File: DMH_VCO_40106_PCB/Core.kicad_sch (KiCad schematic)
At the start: 73 parts, among them Q1 BC558, Q2 BC548, Q7 MMBFJ113, U1 40106, U2 TL074, U3 TL074, U4 TL074

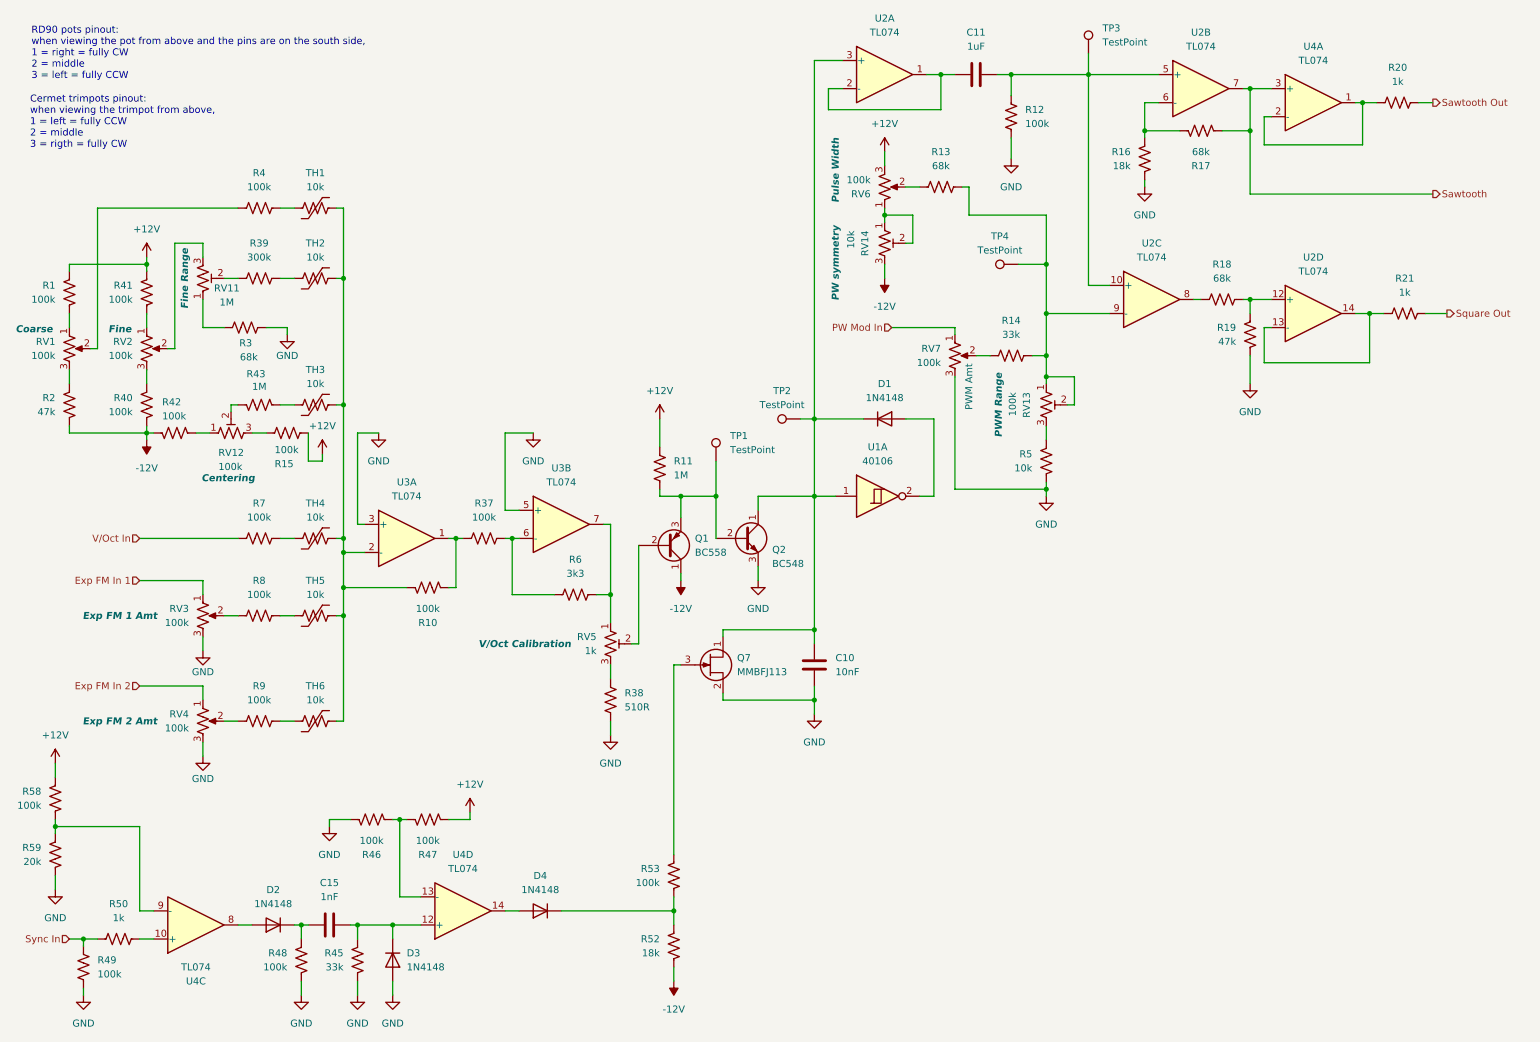
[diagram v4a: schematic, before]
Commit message: Started positioning components on PCB
Moving some input resistores from main PCB to Jacks PCB
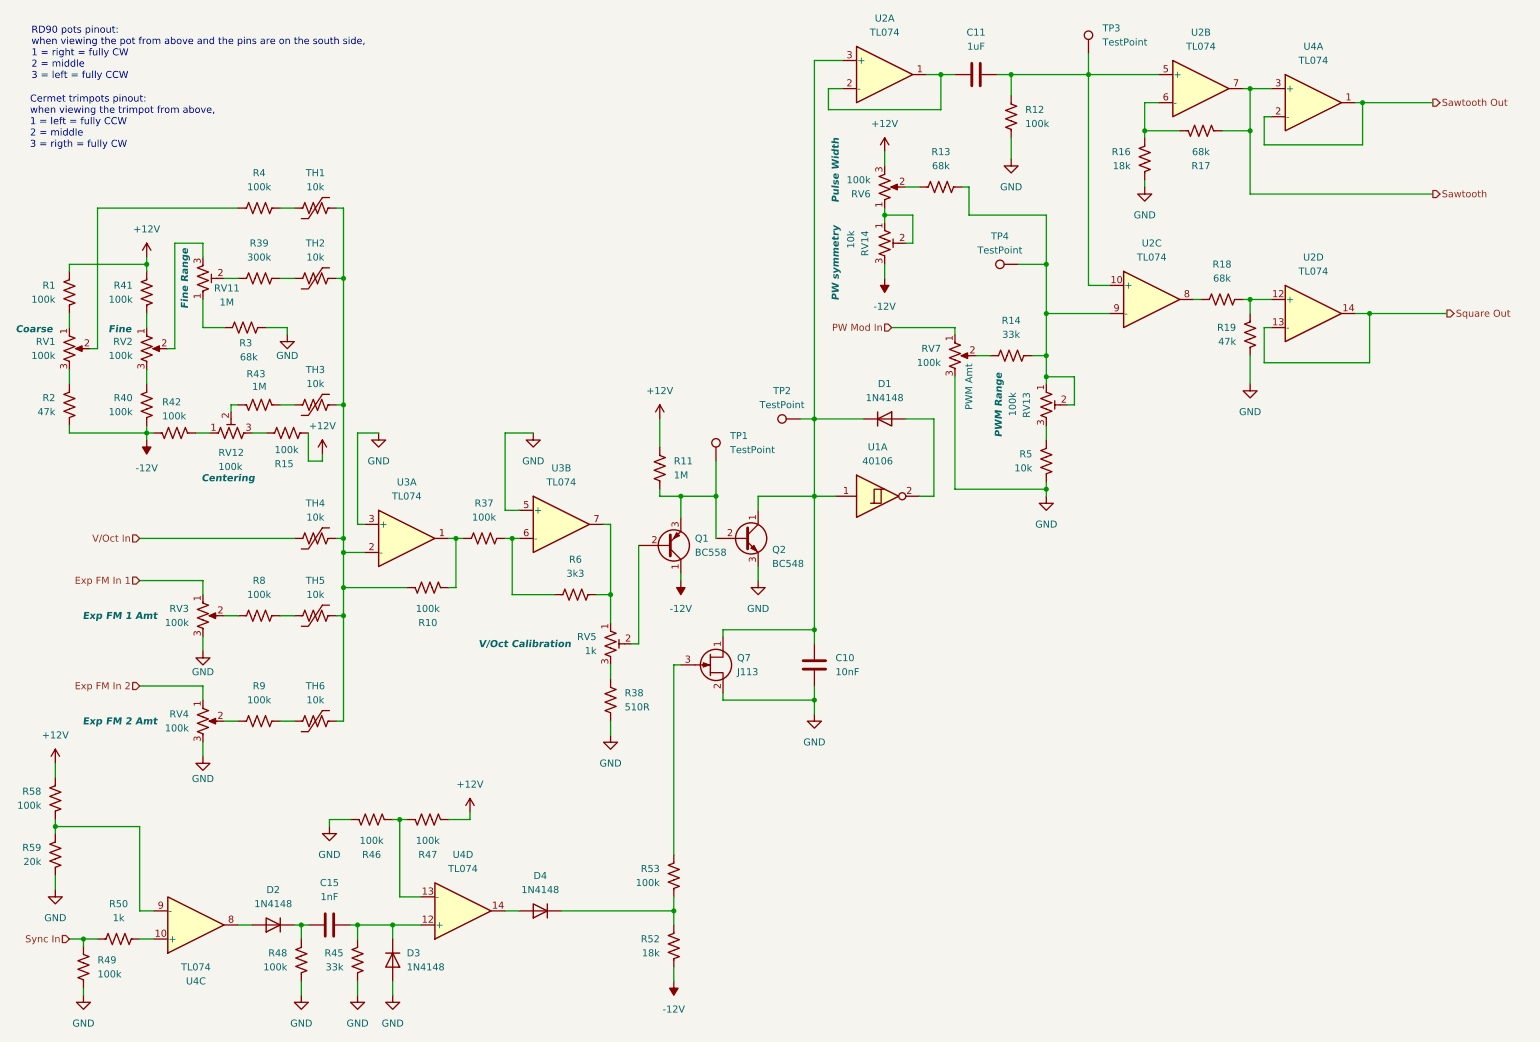
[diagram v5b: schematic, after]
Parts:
- removed R20, R21: 1k, Resistor_THT:R_Axial_DIN0204_L3.6mm_D1.6mm_P5.08mm_Horizontal, symbol Device:R_US
- removed R7: 100k, Resistor_THT:R_Axial_DIN0204_L3.6mm_D1.6mm_P5.08mm_Horizontal, symbol Device:R_US
- C10, C15: footprint (none) -> Capacitor_THT:C_Disc_D3.0mm_W2.0mm_P2.50mm
- C11: footprint (none) -> Capacitor_THT:C_Disc_D4.3mm_W1.9mm_P5.00mm
- Q1, Q2: footprint Package_TO_SOT_THT:TO-92_Inline -> Package_TO_SOT_THT:TO-92_Inline_Wide
- Q7: value MMBFJ113 -> J113; footprint Package_TO_SOT_SMD:SOT-23 -> Package_TO_SOT_THT:TO-92_Inline
- R1, R10, R11, R12, R13, R14, R15, R16, R17, R18, R19, R2, R3, R37, R38, R39, R4, R40, R41, R42, R43, R45, R46, R47, R48, R49, R5, R50, R52, R53, R58, R59, R6, R8, R9: footprint Resistor_THT:R_Axial_DIN0204_L3.6mm_D1.6mm_P5.08mm_Horizontal -> Resistor_THT:R_Axial_DIN0207_L6.3mm_D2.5mm_P7.62mm_Horizontal
- TP1, TP2, TP3, TP4: footprint (none) -> TestPoint:TestPoint_THTPad_2.0x2.0mm_Drill1.0mm; now left out of the parts list
- U4: footprint (none) -> Package_DIP:DIP-14_W7.62mm_Socket
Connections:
- net Sawtooth Out: now also U4.1, U4.2 (-)
- net Square Out: now also U2.13 (-), U2.14
- net V/Oct In: now also TH4.1

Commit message: Component placement ongoing
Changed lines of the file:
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@@
+		)
+	)
+	(text_box "Moved R7=100k to Inputs and Outputs sheet"
+		(exclude_from_sim no)
+		(at 44.45 104.14 0)
+		(size 17.78 7.62)
+		(stroke
+			(width 0)
+			(type default)
+		)
+		(fill
+			(type none)
+		)
+		(effects
+			(font
+				(size 1.27 1.27)
+			)
+			(justify left)
+		)
+	)
+	(text_box "Moved R20=1k to Inputs and Outputs sheet"
+		(exclude_from_sim no)
+		(at 259.08 20.32 0)
+		(size 17.78 7.62)
+		(stroke
+			(width 0)
+			(type default)
+		)
+		(fill
+			(type none)
+		)
+		(effects
+			(font
+				(size 1.27 1.27)
+			)
+			(justify left)
+		)
+	)
+	(text_box "Moved R21=1k to Inputs and Outputs sheet"
+		(exclude_from_sim no)
+		(at 260.35 58.42 0)
+		(size 17.78 7.62)
+		(stroke
+			(width 0)
+			(type default)
+		)
+		(fill
+			(type none)
+		)
+		(effects
+			(font
+				(size 1.27 1.27)
+			)
+			(justify left)
 		)
 	)

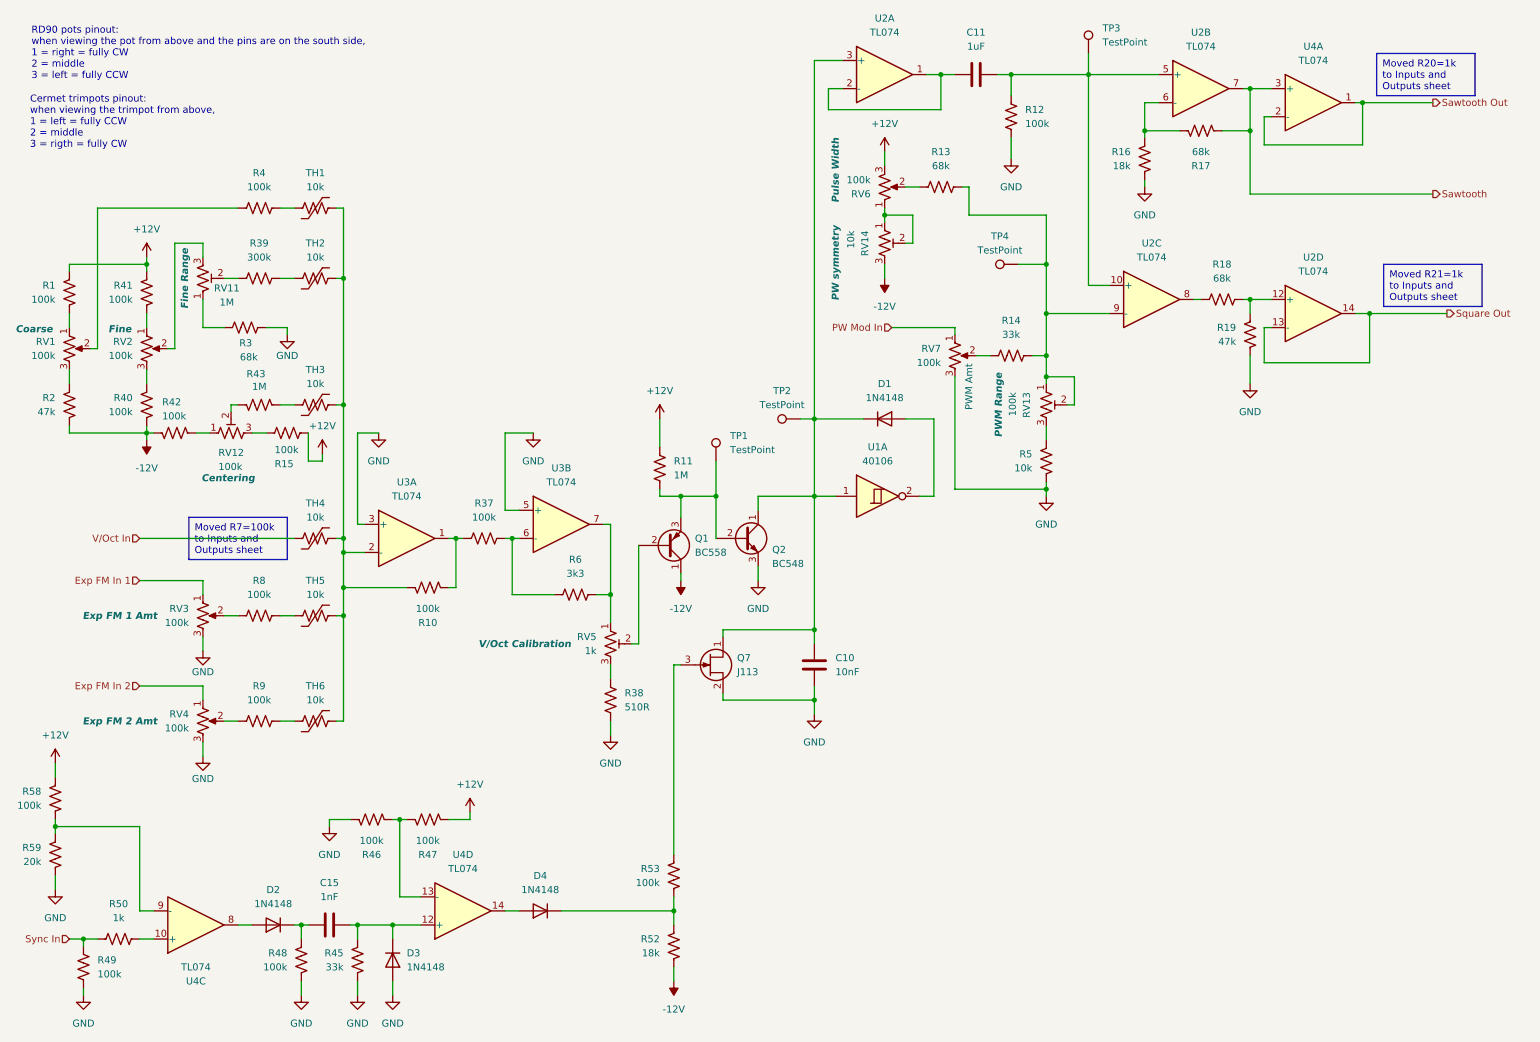
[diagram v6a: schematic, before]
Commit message: Organized Square and Sine Shaper components
Also re-annotated the TL074 ICs to improve the layout
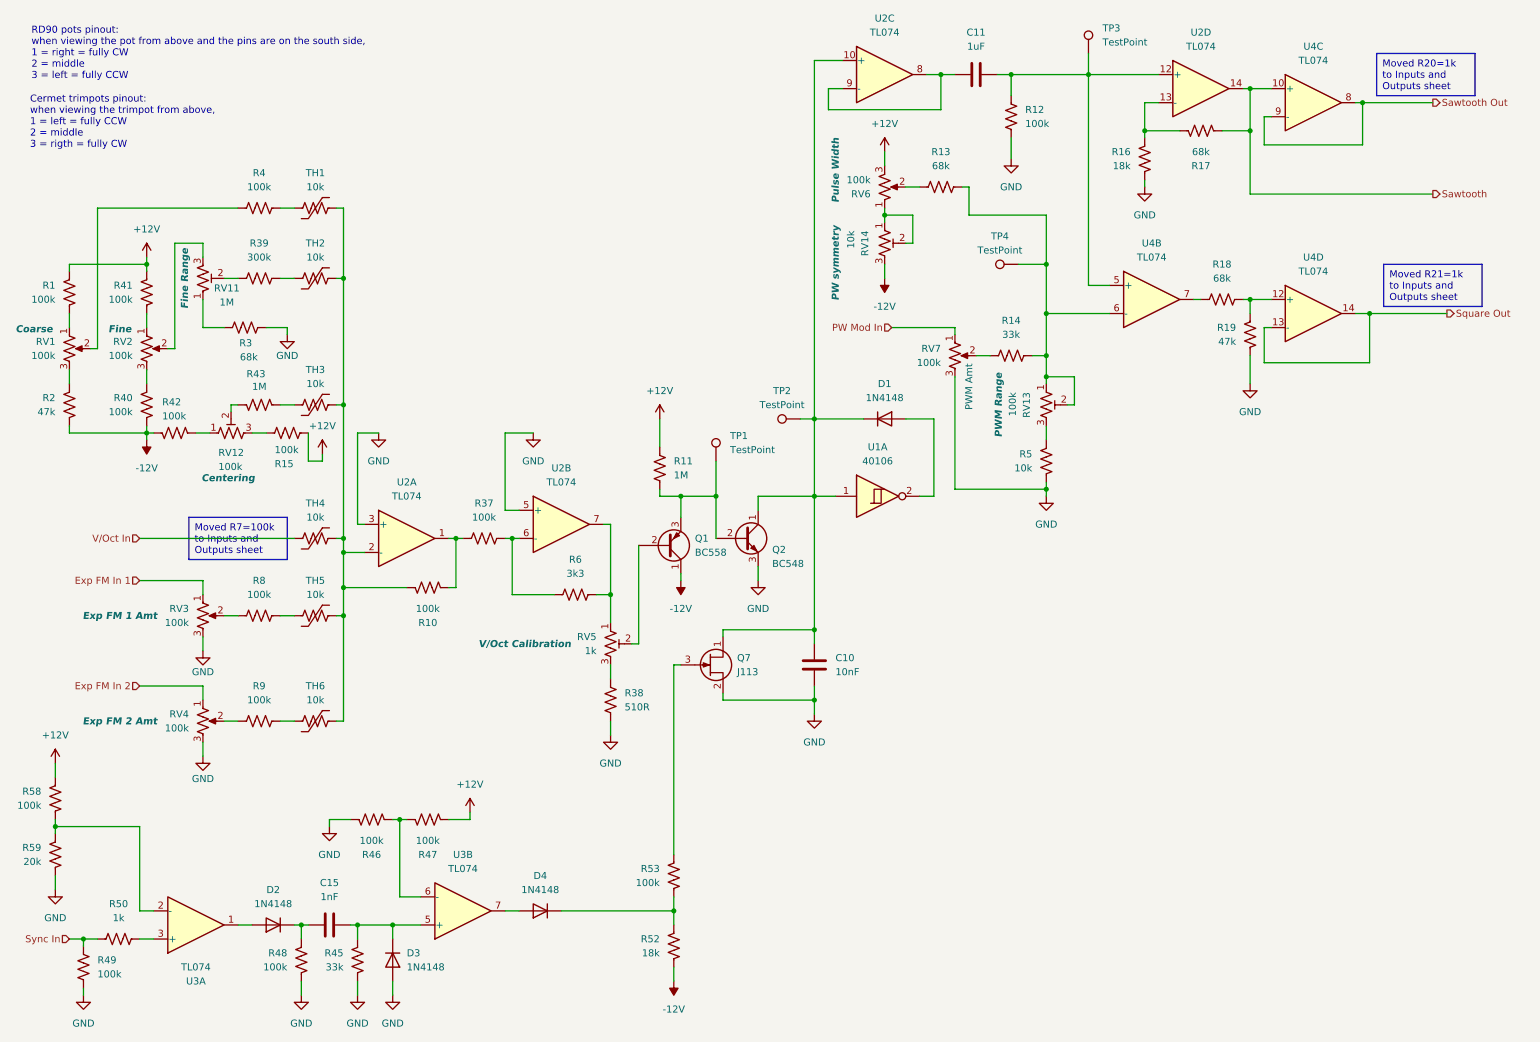
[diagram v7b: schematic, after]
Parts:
- renumbered U3 to U2, U4 to U3, U2 to U4
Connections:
- net Sawtooth: now also U2.14, U4.10 (+); no longer U2.7, U4.3 (+)
- net Sawtooth Out: now also U4.8, U4.9 (-); no longer U4.1, U4.2 (-)
- net at R46.2, R47.1: now also U3.6 (-); no longer U3.13 (-)
- net at C10.1, D1.1 (K), Q2.1 (C)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: now also U2.10 (+); no longer U2.3 (+)
- net at C11.2, R12.2, TP3.1: now also U2.12 (+), U4.5 (+); no longer U2.5 (+), U4.10 (+)
- net at R58.2, R59.1: now also U3.2 (-); no longer U3.9 (-)
- net at R16.2, R17.2: now also U2.13 (-); no longer U2.6 (-)
- net at R50.1: now also U3.3 (+); no longer U3.10 (+)
- net at D2.2 (A): now also U3.1; no longer U3.8
- net at R13.1, R14.1, RV13.1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: now also U4.6 (-); no longer U4.9 (-)
- net at C15.2, D3.1 (K), R45.1: now also U3.5 (+); no longer U3.12 (+)
- net at D4.2 (A): now also U3.7; no longer U3.14
- net at R18.2: now also U4.7; no longer U4.8
- new net: C11.1, U2.8, U2.9 (-)
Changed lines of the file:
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@@
 		(lib_id "Amplifier_Operational:TL074")
 		(at 227.33 26.67 0)
-		(unit 2)
+		(unit 4)
 		(exclude_from_sim no)
 		(in_bom yes)
@@
 			)
 		)
+		(property "Function" ""
+			(at 227.33 26.67 0)
+			(effects
+				(font
+					(size 1.27 1.27)
+				)
+				(hide yes)
+			)
+		)
 		(pin "3"
 		)
@@
 				(path "/fefed352-c100-4617-bbfb-c55e7427b122/681eb850-910f-47de-ab28-b72b47bdbc38"
 					(reference "U2")
-					(unit 2)
+					(unit 4)
 				)
 			)
@@
 		(lib_id "Amplifier_Operational:TL074")
 		(at 170.18 24.13 0)
-		(unit 1)
+		(unit 3)
 		(exclude_from_sim no)
 		(in_bom yes)
@@
 			)
 		)
+		(property "Function" ""
+			(at 170.18 24.13 0)
+			(effects
+				(font
+					(size 1.27 1.27)
+				)
+				(hide yes)
+			)
+		)
 		(pin "3"
 		)
@@
 				(path "/fefed352-c100-4617-bbfb-c55e7427b122/681eb850-910f-47de-ab28-b72b47bdbc38"
 					(reference "U2")
-					(unit 1)
+					(unit 3)
 				)
 			)
@@
 		(at 45.72 177.8 0)
 		(mirror x)
-		(unit 3)
+		(unit 1)
 		(exclude_from_sim no)
 		(in_bom yes)
 		(on_board yes)
 		(dnp no)
-		(property "Reference" "U4"
+		(property "Reference" "U3"
 			(at 45.72 187.96 0)
 			(effects
@@
 			(project ""
 				(path "/fefed352-c100-4617-bbfb-c55e7427b122/681eb850-910f-47de-ab28-b72b47bdbc38"
-					(reference "U4")
-					(unit 3)
+					(reference "U3")
+					(unit 1)
 				)
 			)
@@
 		(lib_id "Amplifier_Operational:TL074")
 		(at 247.65 29.21 0)
-		(unit 1)
+		(unit 3)
 		(exclude_from_sim no)
 		(in_bom yes)
@@
 				(path "/fefed352-c100-4617-bbfb-c55e7427b122/681eb850-910f-47de-ab28-b72b47bdbc38"
 					(reference "U4")
-					(unit 1)
+					(unit 3)
 				)
 			)
@@
 		(at 93.98 175.26 0)
 		(mirror x)
-		(unit 4)
+		(unit 2)
 		(exclude_from_sim no)
 		(in_bom yes)
@@
 		(dnp no)
 		(fields_autoplaced yes)
-		(property "Reference" "U4"
+		(property "Reference" "U3"
 			(at 93.98 165.1 0)
 			(effects
@@
 			(project ""
 				(path "/fefed352-c100-4617-bbfb-c55e7427b122/681eb850-910f-47de-ab28-b72b47bdbc38"
-					(reference "U4")
-					(unit 4)
+					(reference "U3")
+					(unit 2)
 				)
 			)
@@
 		(dnp no)
 		(fields_autoplaced yes)
-		(property "Reference" "U3"
+		(property "Reference" "U2"
 			(at 111.76 95.25 0)
 			(effects
@@
 			(project "DMH_VCO_40106_PCB"
 				(path "/fefed352-c100-4617-bbfb-c55e7427b122/681eb850-910f-47de-ab28-b72b47bdbc38"
-					(reference "U3")
+					(reference "U2")
 					(unit 2)
 				)
@@
 		(dnp no)
 		(fields_autoplaced yes)
-		(property "Reference" "U3"
+		(property "Reference" "U2"
 			(at 83.82 97.79 0)
 			(effects
@@
 			)
 		)
+		(property "Function" ""
+			(at 83.82 107.95 0)
+			(effects
+				(font
+					(size 1.27 1.27)
+				)
+				(hide yes)
+			)
+		)
 		(pin "3"
 		)
@@
 			(project "DMH_VCO_40106_PCB"
 				(path "/fefed352-c100-4617-bbfb-c55e7427b122/681eb850-910f-47de-ab28-b72b47bdbc38"
-					(reference "U3")
+					(reference "U2")
 					(unit 1)
 				)
@@
 		(dnp no)
 		(fields_autoplaced yes)
-		(property "Reference" "U2"
+		(property "Reference" "U4"
 			(at 247.65 57.15 0)
 			(effects
@@
 			)
 		)
+		(property "Function" ""
+			(at 247.65 67.31 0)
+			(effects
+				(font
+					(size 1.27 1.27)
+				)
+				(hide yes)
+			)
+		)
 		(pin "3"
 		)
@@
 			(project "VCO mki PCB"
 				(path "/fefed352-c100-4617-bbfb-c55e7427b122/681eb850-910f-47de-ab28-b72b47bdbc38"
-					(reference "U2")
+					(reference "U4")
 					(unit 4)
 				)
@@
 		(lib_id "Amplifier_Operational:TL074")
 		(at 218.44 64.77 0)
-		(unit 3)
+		(unit 2)
 		(exclude_from_sim no)
 		(in_bom yes)
 		(on_board yes)
 		(dnp no)
-		(property "Reference" "U2"
+		(property "Reference" "U4"
 			(at 218.44 54.61 0)
 			(effects
@@
 			)
 		)
+		(property "Function" ""
+			(at 218.44 64.77 0)
+			(effects
+				(font
+					(size 1.27 1.27)
+				)
+				(hide yes)
+			)
+		)
 		(pin "3"
 		)
@@
 			(project "VCO mki PCB"
 				(path "/fefed352-c100-4617-bbfb-c55e7427b122/681eb850-910f-47de-ab28-b72b47bdbc38"
-					(reference "U2")
-					(unit 3)
+					(reference "U4")
+					(unit 2)
 				)
 			)

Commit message: Finished physical placement
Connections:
- net at R46.2, R47.1: now also U3.13 (-); no longer U3.6 (-)
- net at R58.2, R59.1: now also U3.9 (-); no longer U3.2 (-)
- net at D2.2 (A): now also U3.8; no longer U3.1
- net at R50.1: now also U3.10 (+); no longer U3.3 (+)
- net at C15.2, D3.1 (K), R45.1: now also U3.12 (+); no longer U3.5 (+)
- net at D4.2 (A): now also U3.14; no longer U3.7
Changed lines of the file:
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@@
 		(at 45.72 177.8 0)
 		(mirror x)
-		(unit 1)
+		(unit 3)
 		(exclude_from_sim no)
 		(in_bom yes)
@@
 				(path "/fefed352-c100-4617-bbfb-c55e7427b122/681eb850-910f-47de-ab28-b72b47bdbc38"
 					(reference "U3")
-					(unit 1)
+					(unit 3)
 				)
 			)
@@
 		(at 93.98 175.26 0)
 		(mirror x)
-		(unit 2)
+		(unit 4)
 		(exclude_from_sim no)
 		(in_bom yes)
@@
 				(path "/fefed352-c100-4617-bbfb-c55e7427b122/681eb850-910f-47de-ab28-b72b47bdbc38"
 					(reference "U3")
-					(unit 2)
-				)
-			)
+					(unit 4)
+				)
+			)
